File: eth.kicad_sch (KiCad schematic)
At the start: 43 parts, among them J6 ARJM11C7-114-BA-EW2, U26 LAN8742A, U27 USBLC6-4SC6, Y2 25MHz

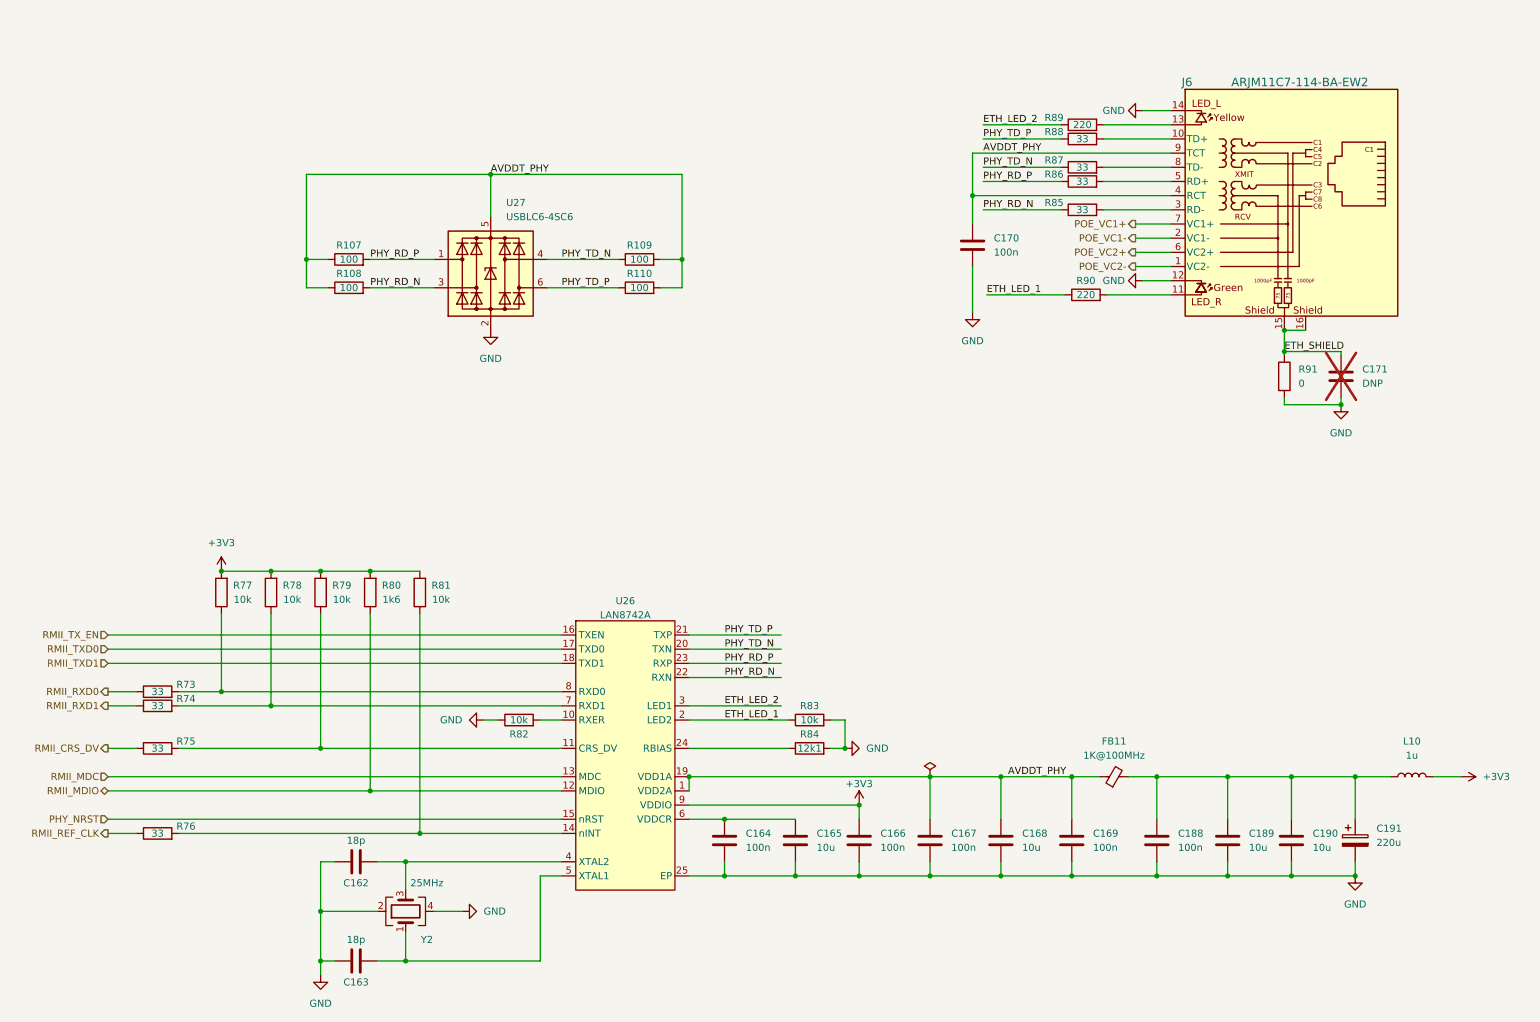
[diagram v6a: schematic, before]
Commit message: pcb: Finish Layout for rev0_3 - Assign MFR_PN for all Components - schematics changes:   - drivestage: Add Switch to optionally enable Modulation Signal Termination   -             Add alternate Precision Power Resistor   -             Modify the RC network values at TIA LPF Output   - MCU: Add Redundant 2.54mm pitch Programming Header   - thermostat: Duplicate the power filter network for alternate Temperature ADC
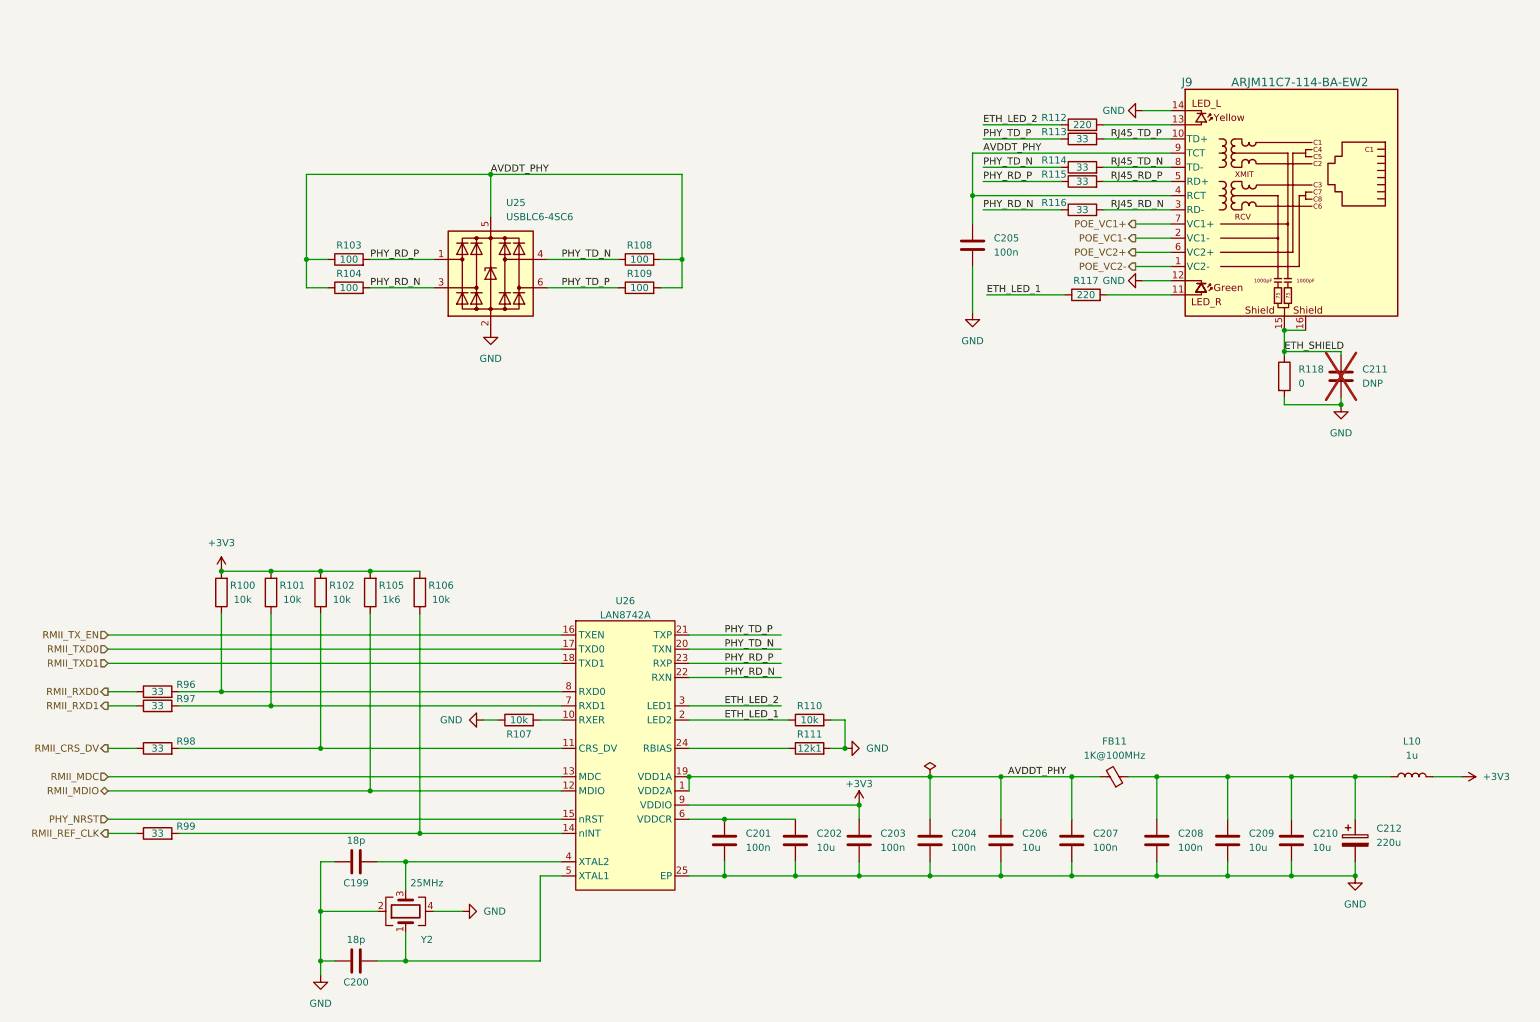
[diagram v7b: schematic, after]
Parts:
- J9: renamed from J6; MFR_PN (none) -> ARJM11C7-114-BA-EW2
- renumbered C162 to C199, C163 to C200, C164 to C201, C165 to C202, C166 to C203, C167 to C204, C170 to C205, C168 to C206, C169 to C207, C188 to C208, C189 to C209, C190 to C210, C171 to C211, C191 to C212, R77 to R100, R78 to R101, R79 to R102, R107 to R103, R108 to R104, R80 to R105, R81 to R106, R82 to R107, R109 to R108, R110 to R109, R83 to R110, R84 to R111, R89 to R112, R88 to R113, R87 to R114, R86 to R115, R85 to R116, R90 to R117, R91 to R118, R73 to R96, R74 to R97, R75 to R98, R76 to R99, U27 to U25
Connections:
- net AVDDT_PHY: now also FB11.2; no longer FB11.1
- net at C208.1, C209.1, C210.1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: now also FB11.1; no longer FB11.2
- net RJ45_RD_N: now reaches J9.3 (RD-), R116.2
- net RJ45_TD_P: now reaches J9.10 (TD+), R113.2
- net RJ45_RD_P: now reaches J9.5 (RD+), R115.2
- net RJ45_TD_N: now reaches J9.8 (TD-)
- net RJ45_TD_N: now also R114.2
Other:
- moved on the sheet: FB11

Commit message: sch: Update Title Block Info - rev0.3 -> rev0_3 - Correct the title of each schematics - Update the modified time
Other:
- company: M-Labs -> M-Labs Limited
- title: Kirdy -> Ethernet
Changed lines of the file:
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@@
   (paper "A3")
   (title_block
-    (title "Kirdy")
-    (date "2022-07-03")
-    (rev "r0.3")
-    (company "M-Labs")
+    (title "Ethernet")
+    (date "2023-11-09")
+    (rev "r0_3")
+    (company "M-Labs Limited")
     (comment 1 "Linus Woo Chun Kit")
   )
